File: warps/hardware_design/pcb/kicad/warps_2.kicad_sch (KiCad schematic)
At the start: 56 parts

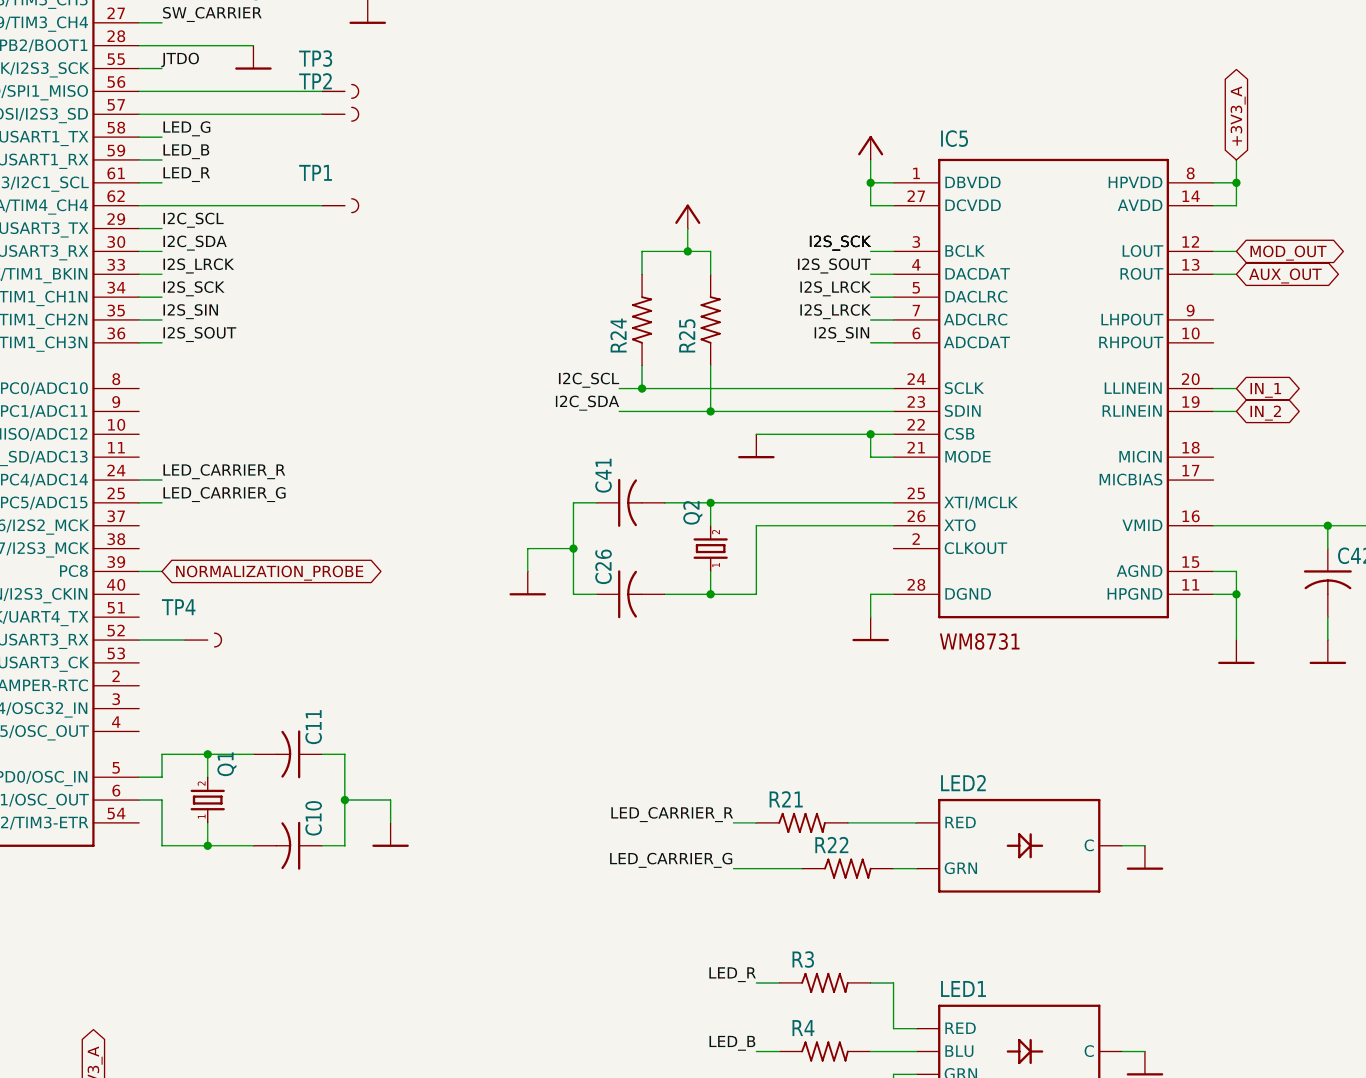
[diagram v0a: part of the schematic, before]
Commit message: warps caps + wm8731
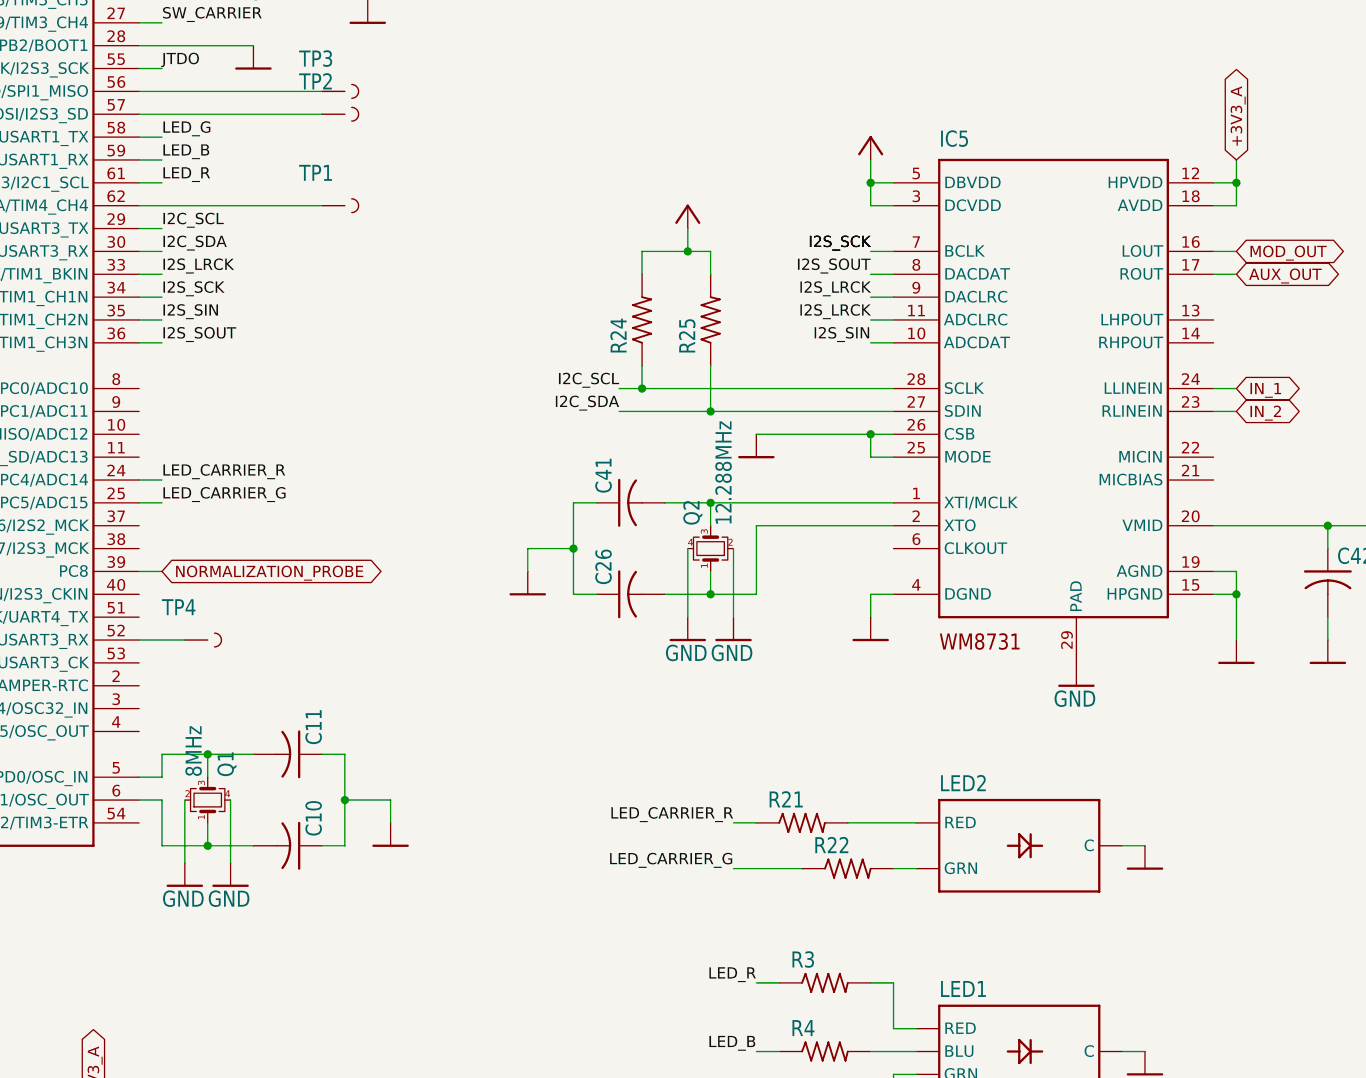
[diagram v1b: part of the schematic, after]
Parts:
- removed IC5: (no value), symbol warps-eagle-import:WM8731
- added IC5: WM8731, Package_DFN_QFN:QFN-28-1EP_5x5mm_P0.5mm_EP3.35x3.35mm, symbol clouds-eagle-import:WM8731
- C23, C29, C36: footprint (none) -> plaits:PANASONIC_B
- Q1: value (none) -> 8MHz; footprint (none) -> Crystal:Crystal_SMD_3225-4Pin_3.2x2.5mm; symbol warps-eagle-import:CRYSTALHC49UP -> Device:Crystal_GND24_Small
- Q2: value (none) -> 12.288MHz; footprint (none) -> Crystal:Crystal_SMD_5032-4Pin_5.0x3.2mm; symbol warps-eagle-import:CRYSTALHC49UP -> Device:Crystal_GND24_Small
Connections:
- net +3V3: now also IC5.3 (DCVDD), IC5.5 (DBVDD)
- net +3V3_A: now also IC5.12 (HPVDD), IC5.18 (AVDD)
- net AUX_OUT: now also IC5.17 (ROUT)
- net GND: now also Q1.2, Q1.4, Q2.2, Q2.4, IC5.15 (HPGND), IC5.19 (AGND), IC5.25 (MODE), IC5.26 (CSB), IC5.29 (PAD), IC5.4 (DGND)
- net I2C_SCL: now also IC5.28 (SCLK)
- net I2C_SDA: now also IC5.27 (SDIN)
- net I2S_LRCK: now also IC5.11 (ADCLRC), IC5.9 (DACLRC)
- net I2S_SCK: now also IC5.7 (BCLK)
- net I2S_SIN: now also IC5.10 (ADCDAT)
- net I2S_SOUT: now also IC5.8 (DACDAT)
- net IN_1: now also IC5.24 (LLINEIN)
- net IN_2: now also IC5.23 (RLINEIN)
- net MOD_OUT: now also IC5.16 (LOUT)
- net at C11.2, IC4.5 (PD0/OSC_IN): now also Q1.3; no longer Q1.2
- net at C26.2, Q2.1: now also IC5.2 (XTO)
- net at C41.2: now also Q2.3, IC5.1 (XTI/MCLK); no longer Q2.2
- net at C36.+, C42.1: now also IC5.20 (VMID)

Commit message: warps SMD boot/reset buttons
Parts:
- C10, C11, C26, C41: value (none) -> 18p; footprint (none) -> warps:C0603
- C15, C27: value (none) -> 1u; footprint (none) -> warps:C0603
- C16, C17, C18, C20, C21, C24, C25, C28, C30, C31, C33, C42, C9: value (none) -> 100n; footprint (none) -> warps:C0603
- C19, C22: value (none) -> 2.2u; footprint (none) -> warps:C0805
- C23, C29, C36: value (none) -> 10u
- F1, F2, F3, F4: value (none) -> FIDUCIAL1X2; footprint (none) -> warps:FIDUCIAL-1X2
- IC4: value (none) -> STM32F405RGT6; footprint (none) -> warps:TQFP-10X10-64
- JP1: value (none) -> M05X2MINIJTAG; footprint (none) -> warps:2X5-1.27
- JP2: value (none) -> M06SIP; footprint (none) -> warps:1X06
- LED1: value (none) -> WP154A4SUREQBFZG; footprint (none) -> warps:LED-TRICOLOR-THROUGHHOLE
- LED2: value (none) -> WP115VEGW; footprint (none) -> warps:LED-BICOLOR-THROUGHHOLE
- R14, R2: value (none) -> 10k; footprint (none) -> warps:R0603
- R21, R22: value (none) -> 180; footprint (none) -> warps:R0603
- R23, R7: value (none) -> 10kB; footprint (none) -> warps:ALPS_POT_VERTICAL_PS
- R24, R25: value (none) -> 2.2k; footprint (none) -> warps:R0603
- R26, R27: value (none) -> 10kB; footprint (none) -> warps:ALPS_POT_VERTICAL
- R3, R4, R5: value (none) -> 100; footprint (none) -> warps:R0603
- SW1, SW2: value (none) -> EVQQ2; footprint (none) -> Supercell 1.3:k2-1808 pushbutton switch
- SW3: value (none) -> TAC_SWITCHPTH; footprint (none) -> warps:TACTILE-PTH
- TP1, TP2, TP3, TP4: value (none) -> TEST-POINT3X5; footprint (none) -> warps:PAD.03X.05
